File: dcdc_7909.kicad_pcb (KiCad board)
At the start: 4 copper layers, 41.5 x 27 mm, 48 parts, among them J1 V_IN, J2 G_IN, J3 Conn_01x01, J4 Conn_01x01, J5 Conn_01x01, J6 Conn_01x01, J7 +10V, J8 G_OUT, J9 -10V, U1 LM2940-SOT223-15, U2 MAX764, U3 LT3045xMSE, U4 LT3094xMSE

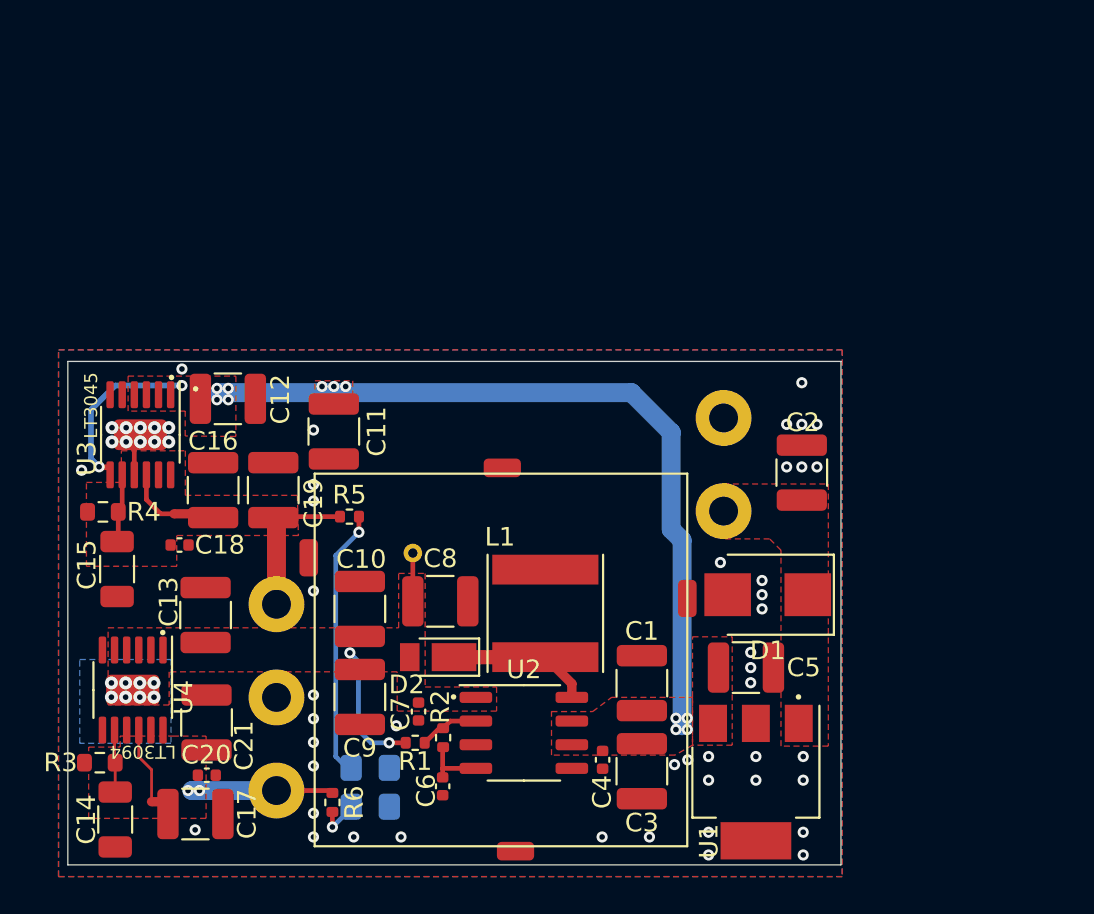
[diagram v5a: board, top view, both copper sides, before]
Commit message: Ready design, but MAX764 cannot be used because of the Vin-Vout differential.
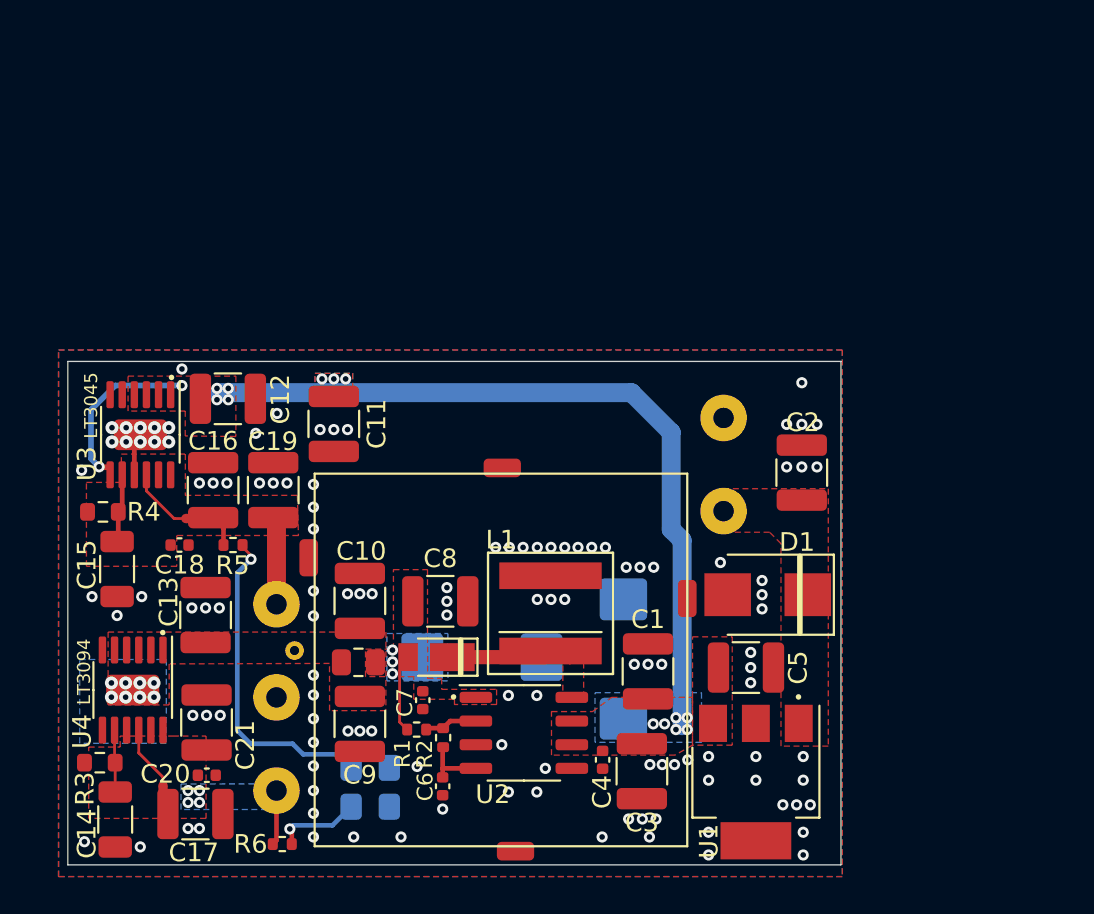
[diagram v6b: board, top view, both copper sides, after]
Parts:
- added C22: C_Polarized_Small, Capacitor_Tantalum_SMD:CP_EIA-7343-31_Kemet-D_Pad2.25x2.55mm_HandSolder, B.Cu at (107.8, 70.0)
- added C23: C_Polarized_Small, Capacitor_Tantalum_SMD:CP_EIA-7343-31_Kemet-D_Pad2.25x2.55mm_HandSolder, B.Cu at (100.2, 69.8)
- added FB1: FerriteBead_Small, Resistor_SMD:R_0805_2012Metric, F.Cu at (93.6, 70.1)
- L1: footprint Inductor_SMD:L_Taiyo-Yuden_NR-60xx -> marcin_library:IND_XGL6060-103MEC
- moved TP1 8.23 mm to (90.2, 69.5)
- moved R5 6.43 mm to (86.9, 63.8)
- moved R6 3.50 mm to (89.5, 79.9), turned to 0 degrees
- moved C9 1.45 mm to (93.7, 73.4)
- moved R1 0.72 mm to (96.7, 73.7)
- moved C1 0.71 mm to (109.1, 70.6)
- moved NT1 0.68 mm to (84.8, 62.4)
- moved C7 0.65 mm to (97.1, 72.2)
- moved C10 0.43 mm to (93.7, 66.8)
- moved C11 0.41 mm to (92.3, 57.3)
- moved NT2 0.39 mm to (83.1, 77.2), turned to -90 degrees
- moved L1 0.28 mm to (103.9, 67.5)
- moved D2 0.09 mm to (97.8, 69.8)
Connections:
- C7 pad 1: /-10.7 -> Net-(C23-Pad1)
- C8 pad 1: /-10.7 -> Net-(C23-Pad1)
- D2 pad 2: /-10.7 -> Net-(C23-Pad1)
- R1 pad 2: /-10.7 -> Net-(C23-Pad1)
- U2 pad 1: /-10.7 -> Net-(C23-Pad1)
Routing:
- net /-10.7: track 9.86 -> 0.00 mm, vias 10 -> 8
- net /-10V: track 7.60 -> 2.96 mm, vias 2 -> 4
- net Net-(C23-Pad1): track 0.00 -> 3.34 mm, vias 0 -> 3
- net Net-(D3-Pad2): track 14.6 -> 17.4 mm
- net Net-(D4-Pad1): track 2.32 -> 4.64 mm
- net /+10V: track 8.33 -> 6.42 mm
- net Net-(D2-Pad1): track 7.65 -> 6.22 mm
- net Net-(NT2-Pad1): track 4.13 -> 3.42 mm
- net VCC: vias 13 -> 15
- net GND: vias 54 -> 122
- added copper zone on B.Cu, net /-10V
- added copper zone on B.Cu, net Net-(C23-Pad1)
- added copper zone on F.Cu, net Net-(C23-Pad1)
- added copper zone on F.Cu, net Net-(D2-Pad1)
- added copper zone on B.Cu, net VCC
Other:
- board text added: "+"
- board text added: "+10V"
- board text added: "-10V"

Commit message: Switched to MAX77x + Si9435.
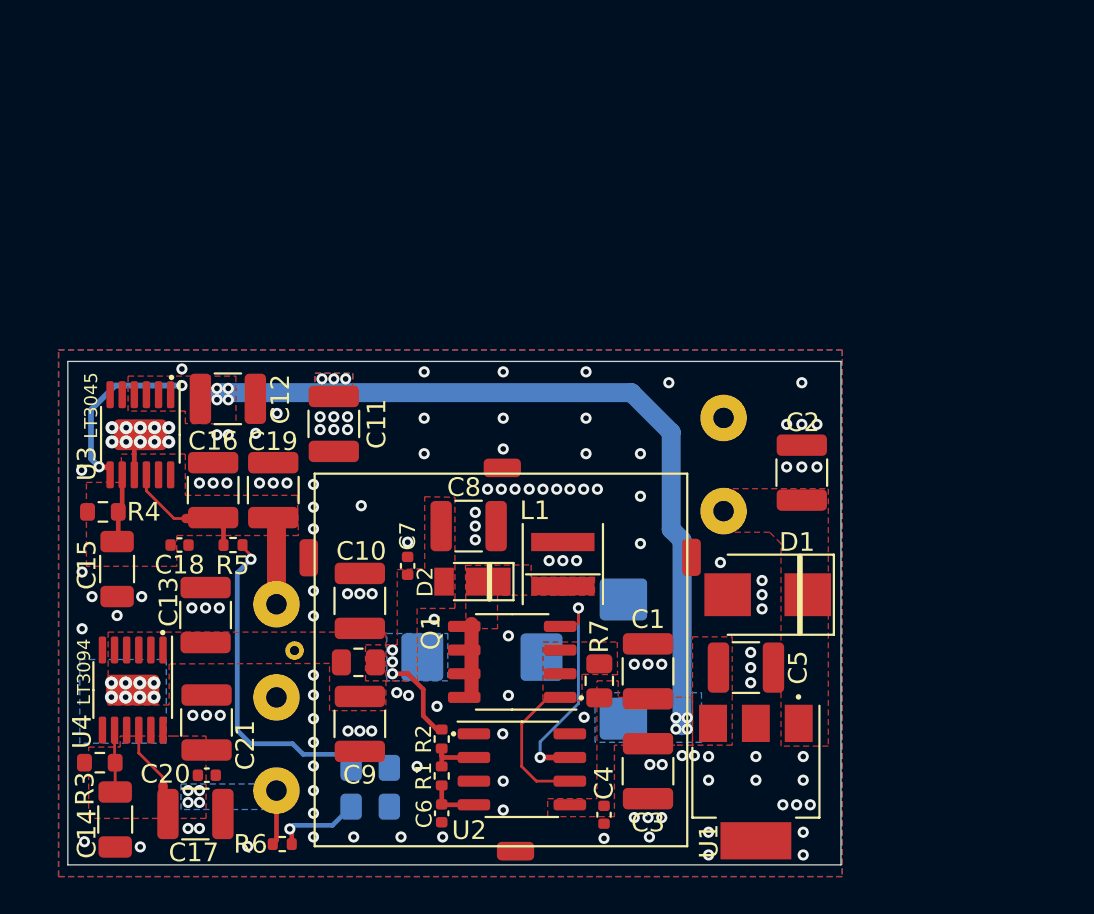
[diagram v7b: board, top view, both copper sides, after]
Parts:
- added Q1: Si9435, Package_SO:SO-8_3.9x4.9mm_P1.27mm, F.Cu at (101.9, 70.1)
- added R7: 0R1, Resistor_SMD:R_0805_2012Metric, F.Cu at (106.5, 71.1)
- C23: value C_Polarized_Small -> 100u
- L1: value 47u -> 22u; footprint marcin_library:IND_XGL6060-103MEC -> Inductor_SMD:L_Coilcraft_XxL4040
- U2: value MAX764 -> MAX774
- moved C7 7.26 mm to (96.2, 64.9), turned to 90 degrees
- moved D2 4.49 mm to (99.7, 65.8)
- moved C8 4.32 mm to (99.5, 62.8)
- moved C4 2.95 mm to (106.8, 78.3)
- moved L1 2.73 mm to (104.6, 64.9)
- moved J4 2.22 mm to (111.5, 64.5)
- moved R1 2.06 mm to (98.1, 76.2)
- moved U2 1.96 mm to (102.4, 75.9)
- moved C6 1.45 mm to (98.1, 78.2)
- moved R2 1.44 mm to (98.1, 74.2), turned to 90 degrees
- moved C3 0.33 mm to (109.1, 76.0)
- renumbered R2 to R1, R1 to R2
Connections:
- net Net-(C6-Pad1) renamed /REF
- U2 pad 1: Net-(C23-Pad1) -> GND
- U2 pad 5: GND -> VCC
- U2 pad 6: VCC -> /CS
- U2 pad 7: VCC -> /EXT
- U2 pad 8: Net-(D2-Pad1) -> GND
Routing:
- net /EXT: track 0.00 -> 11.4 mm, vias 0 -> 2
- net /CS: track 0.00 -> 7.39 mm
- net Net-(C23-Pad1): track 3.34 -> 4.87 mm
- net Net-(D2-Pad1): track 6.22 -> 4.86 mm
- net /REF: track 3.31 -> 2.75 mm
- net VCC: vias 15 -> 13
- net GND: vias 122 -> 146
- added copper zone on F.Cu, net /CS
